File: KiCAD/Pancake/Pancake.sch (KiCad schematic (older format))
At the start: 40 parts, among them IC3 LF347N, J1 Conn_01x08_Male, J101 TB001-500-04BE, J102 TB001-500-03BE, J2 Conn_01x08_Male, J3 Conn_01x08_Male, J4 Conn_01x08_Male, J5 Conn_01x08_Male, J7 Conn_02x15_Top_Bottom

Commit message: Latest revision
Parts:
- IC3: symbol SamacSys_Parts:LF347N -> Pancake-rescue:LF347N-SamacSys_Parts
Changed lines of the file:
@@
 ADC0
 $Comp
-L SamacSys_Parts:LF347N IC3
+L Pancake-rescue:LF347N-SamacSys_Parts IC3
 U 1 1 612701DD
 P 3725 2975

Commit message: Lib updates and capacitor add. Simulation on power resistor working
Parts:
- added C101: 220nF, Capacitor_THT:CP_Radial_D16.0mm_P7.50mm, symbol Device:C
- IC3: footprint DIP794W56P254L1905H533Q14N -> SamacSys_Parts:DIP794W56P254L1905H533Q14N; symbol Pancake-rescue:LF347N-SamacSys_Parts -> SamacSys_Parts:LF347N
- J101: footprint TB00150004BE -> SamacSys_Parts:TB00150004BE; symbol Pancake-rescue:TB001-500-04BE-SamacSys_Parts -> SamacSys_Parts:TB001-500-04BE
- J102: footprint TB00150003BE -> SamacSys_Parts:TB00150003BE; symbol Pancake-rescue:TB001-500-03BE-SamacSys_Parts -> SamacSys_Parts:TB001-500-03BE
- R101: footprint TO508P438X1010X1539-2P -> SamacSys_Parts:TO508P438X1010X1539-2P; symbol Pancake-rescue:PWR220T-35-8R00F-SamacSys_Parts -> SamacSys_Parts:PWR220T-35-8R00F
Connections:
- wire segments 75 -> 79
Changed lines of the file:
@@
 Text Label 6500 7075 0    50   ~ 0
 AuxIn
-Text Label 4175 4625 2    50   ~ 0
+Text Label 4175 4475 2    50   ~ 0
 SPRKPos
 Text Label 8400 3625 2    50   ~ 0
 8VOut
-Text Label 4175 5575 2    50   ~ 0
+Text Label 4175 5775 2    50   ~ 0
 SPRKNeg
 Wire Wire Line
@@
 ADC0
 $Comp
-L Pancake-rescue:LF347N-SamacSys_Parts IC3
+L SamacSys_Parts:LF347N IC3
 U 1 1 612701DD
 P 3725 2975
 F 0 "IC3" H 4275 3240 50  0000 C CNN
 F 1 "LF347N" H 4275 3149 50  0000 C CNN
-F 2 "DIP794W56P254L1905H533Q14N" H 4675 3075 50  0001 L CNN
+F 2 "SamacSys_Parts:DIP794W56P254L1905H533Q14N" H 4675 3075 50  0001 L CNN
 F 3 "http://www.ti.com/lit/ds/symlink/lf347-n.pdf" H 4675 2975 50  0001 L CNN
 F 4 "Quad General-Purpose JFET-input Operational Amplifier" H 4675 2875 50  0001 L CNN "Description"
@@
 PresenceOut
 $Comp
-L Pancake-rescue:PWR220T-35-8R00F-SamacSys_Parts R101
+L SamacSys_Parts:PWR220T-35-8R00F R101
 U 1 1 614C8890
-P 4525 5425
-F 0 "R101" H 4875 5650 50  0000 C CNN
-F 1 "PWR220T-35-8R00F" H 4875 5559 50  0000 C CNN
-F 2 "TO508P438X1010X1539-2P" H 5075 5475 50  0001 L CNN
-F 3 "https://componentsearchengine.com/Datasheets/1/PWR220T-35-8R00F.pdf" H 5075 5375 50  0001 L CNN
-F 4 "Thick Film Resistors - Through Hole 8ohm 35W 1% TOL Thru Hole" H 5075 5275 50  0001 L CNN "Description"
-F 5 "4.38" H 5075 5175 50  0001 L CNN "Height"
-F 6 "Bourns" H 5075 5075 50  0001 L CNN "Manufacturer_Name"
-F 7 "PWR220T-35-8R00F" H 5075 4975 50  0001 L CNN "Manufacturer_Part_Number"
-F 8 "652-PWR220T-35-8R00F" H 5075 4875 50  0001 L CNN "Mouser Part Number"
-F 9 "http://www.mouser.com/Search/ProductDetail.aspx?qs=Zq5ylnUbLm6EF6%252bwjhnGig%3d%3d" H 5075 4775 50  0001 L CNN "Mouser Price/Stock"
-F 10 "" H 5075 4675 50  0001 L CNN "Arrow Part Number"
-F 11 "" H 5075 4575 50  0001 L CNN "Arrow Price/Stock"
-	1    4525 5425
+P 4525 5625
+F 0 "R101" H 4875 5850 50  0000 C CNN
+F 1 "PWR220T-35-8R00F" H 4875 5759 50  0000 C CNN
+F 2 "SamacSys_Parts:TO508P438X1010X1539-2P" H 5075 5675 50  0001 L CNN
+F 3 "https://componentsearchengine.com/Datasheets/1/PWR220T-35-8R00F.pdf" H 5075 5575 50  0001 L CNN
+F 4 "Thick Film Resistors - Through Hole 8ohm 35W 1% TOL Thru Hole" H 5075 5475 50  0001 L CNN "Description"
+F 5 "4.38" H 5075 5375 50  0001 L CNN "Height"
+F 6 "Bourns" H 5075 5275 50  0001 L CNN "Manufacturer_Name"
+F 7 "PWR220T-35-8R00F" H 5075 5175 50  0001 L CNN "Manufacturer_Part_Number"
+F 8 "652-PWR220T-35-8R00F" H 5075 5075 50  0001 L CNN "Mouser Part Number"
+F 9 "http://www.mouser.com/Search/ProductDetail.aspx?qs=Zq5ylnUbLm6EF6%252bwjhnGig%3d%3d" H 5075 4975 50  0001 L CNN "Mouser Price/Stock"
+F 10 "" H 5075 4875 50  0001 L CNN "Arrow Part Number"
+F 11 "" H 5075 4775 50  0001 L CNN "Arrow Price/Stock"
+	1    4525 5625
 	0    -1   -1   0
 $EndComp
@@
 $EndComp
 $Comp
-L Pancake-rescue:TB001-500-04BE-SamacSys_Parts J101
+L SamacSys_Parts:TB001-500-04BE J101
 U 1 1 6131A74D
 P 1300 4550
 F 0 "J101" H 1592 3985 50  0000 C CNN
 F 1 "TB001-500-04BE" H 1592 4076 50  0000 C CNN
-F 2 "TB00150004BE" H 1950 4650 50  0001 L CNN
+F 2 "SamacSys_Parts:TB00150004BE" H 1950 4650 50  0001 L CNN
 F 3 "https://componentsearchengine.com/Datasheets/1/TB001-500-04BE.pdf" H 1950 4550 50  0001 L CNN
 F 4 "Fixed Terminal Blocks Terminal block, screw type, 5.00, horizontal, 4 poles, CUI Blue, slotted screw, PCB mount" H 1950 4450 50  0001 L CNN "Description"
@@
 $EndComp
 Wire Wire Line
-	4900 4700 4525 4700
-Wire Wire Line
-	4525 4700 4525 4725
-Wire Wire Line
-	4525 5425 4900 5425
-Wire Wire Line
-	4175 4625 4525 4625
-Wire Wire Line
-	4525 4625 4525 4700
-Connection ~ 4525 4700
-Wire Wire Line
-	4175 5575 4525 5575
-Wire Wire Line
-	4525 5575 4525 5425
-Connection ~ 4525 5425
-$Comp
-L Pancake-rescue:TB001-500-03BE-SamacSys_Parts J102
+	4175 4475 4525 4475
+Wire Wire Line
+	4525 4475 4525 4550
+Wire Wire Line
+	4175 5775 4525 5775
+Wire Wire Line
+	4525 5775 4525 5625
+$Comp
+L SamacSys_Parts:TB001-500-03BE J102
 U 1 1 6151F148
 P 2600 4525
 F 0 "J102" H 2892 4060 50  0000 C CNN
 F 1 "TB001-500-03BE" H 2892 4151 50  0000 C CNN
-F 2 "TB00150003BE" H 3250 4625 50  0001 L CNN
+F 2 "SamacSys_Parts:TB00150003BE" H 3250 4625 50  0001 L CNN
 F 3 "https://www.cuidevices.com/product/resource/tb001-500.pdf" H 3250 4525 50  0001 L CNN
 F 4 "Fixed Terminal Blocks screw type, 5.00, horizontal, 3 poles, CUI Blue, slotted screw, PCB mount" H 3250 4425 50  0001 L CNN "Description"
@@
 	0    1    1    0
 $EndComp
+$Comp
+L Device:C C?
+U 1 1 613EF2BB
+P 4525 4700
+AR Path="/61024B6A/613EF2BB" Ref="C?"  Part="1"
+AR Path="/612AE90B/613EF2BB" Ref="C?"  Part="1"
+AR Path="/613EF2BB" Ref="C101"  Part="1"
+F 0 "C101" V 4273 4700 50  0000 C CNN
+F 1 "220nF" V 4364 4700 50  0000 C CNN
+F 2 "Capacitor_THT:CP_Radial_D16.0mm_P7.50mm" H 4563 4550 50  0001 C CNN
+F 3 "~" H 4525 4700 50  0001 C CNN
+	1    4525 4700
+	1    0    0    -1
+$EndComp
+Wire Wire Line
+	4525 4850 4525 4925
+Wire Wire Line
+	4900 4700 4825 4700
+Wire Wire Line
+	4825 4700 4825 4475
+Wire Wire Line
+	4825 4475 4525 4475
+Connection ~ 4525 4475
+Wire Wire Line
+	4900 5425 4825 5425
+Wire Wire Line
+	4825 5425 4825 5775
+Wire Wire Line
+	4825 5775 4525 5775
+Connection ~ 4525 5775
 $EndSCHEMATC

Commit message: The traces is all that is left. we may fall into problems with mark with clearances, we will see.
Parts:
- removed R101: PWR220T-35-8R00F, SamacSys_Parts:TO508P438X1010X1539-2P, symbol SamacSys_Parts:PWR220T-35-8R00F
- added R85, R86: 10, Resistor_THT:R_Axial_Power_L48.0mm_W12.5mm_P55.88mm, symbol Device:R
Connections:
- wire segments 79 -> 85
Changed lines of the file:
@@
 ADC0
-$Comp
-L SamacSys_Parts:LF347N IC3
-U 1 1 612701DD
-P 3725 2975
-F 0 "IC3" H 4275 3240 50  0000 C CNN
-F 1 "LF347N" H 4275 3149 50  0000 C CNN
-F 2 "SamacSys_Parts:DIP794W56P254L1905H533Q14N" H 4675 3075 50  0001 L CNN
-F 3 "http://www.ti.com/lit/ds/symlink/lf347-n.pdf" H 4675 2975 50  0001 L CNN
-F 4 "Quad General-Purpose JFET-input Operational Amplifier" H 4675 2875 50  0001 L CNN "Description"
-F 5 "5.334" H 4675 2775 50  0001 L CNN "Height"
-F 6 "Texas Instruments" H 4675 2675 50  0001 L CNN "Manufacturer_Name"
-F 7 "LF347N" H 4675 2575 50  0001 L CNN "Manufacturer_Part_Number"
-F 8 "595-LF347N" H 4675 2475 50  0001 L CNN "Mouser Part Number"
-F 9 "https://www.mouser.co.uk/ProductDetail/Texas-Instruments/LF347N?qs=DcvZ7Fltd5zOlQRQ%252BiS7vA%3D%3D" H 4675 2375 50  0001 L CNN "Mouser Price/Stock"
-F 10 "LF347N" H 4675 2275 50  0001 L CNN "Arrow Part Number"
-F 11 "https://www.arrow.com/en/products/lf347n/texas-instruments" H 4675 2175 50  0001 L CNN "Arrow Price/Stock"
-	1    3725 2975
-	1    0    0    -1
-$EndComp
 $Comp
 L Device:R R?
@@
 Text Label 3775 1975 0    50   ~ 0
 PresenceOut
-$Comp
-L SamacSys_Parts:PWR220T-35-8R00F R101
-U 1 1 614C8890
-P 4525 5625
-F 0 "R101" H 4875 5850 50  0000 C CNN
-F 1 "PWR220T-35-8R00F" H 4875 5759 50  0000 C CNN
-F 2 "SamacSys_Parts:TO508P438X1010X1539-2P" H 5075 5675 50  0001 L CNN
-F 3 "https://componentsearchengine.com/Datasheets/1/PWR220T-35-8R00F.pdf" H 5075 5575 50  0001 L CNN
-F 4 "Thick Film Resistors - Through Hole 8ohm 35W 1% TOL Thru Hole" H 5075 5475 50  0001 L CNN "Description"
-F 5 "4.38" H 5075 5375 50  0001 L CNN "Height"
-F 6 "Bourns" H 5075 5275 50  0001 L CNN "Manufacturer_Name"
-F 7 "PWR220T-35-8R00F" H 5075 5175 50  0001 L CNN "Manufacturer_Part_Number"
-F 8 "652-PWR220T-35-8R00F" H 5075 5075 50  0001 L CNN "Mouser Part Number"
-F 9 "http://www.mouser.com/Search/ProductDetail.aspx?qs=Zq5ylnUbLm6EF6%252bwjhnGig%3d%3d" H 5075 4975 50  0001 L CNN "Mouser Price/Stock"
-F 10 "" H 5075 4875 50  0001 L CNN "Arrow Part Number"
-F 11 "" H 5075 4775 50  0001 L CNN "Arrow Price/Stock"
-	1    4525 5625
-	0    -1   -1   0
-$EndComp
 $Comp
 L power:+12V #PWR0116
@@
 Wire Wire Line
 	4175 5775 4525 5775
-Wire Wire Line
-	4525 5775 4525 5625
 $Comp
 L SamacSys_Parts:TB001-500-03BE J102
@@
 $EndComp
 Wire Wire Line
-	4525 4850 4525 4925
-Wire Wire Line
 	4900 4700 4825 4700
 Wire Wire Line
@@
 	4825 5775 4525 5775
 Connection ~ 4525 5775
+$Comp
+L SamacSys_Parts:LF347N IC3
+U 1 1 612701DD
+P 3725 2975
+F 0 "IC3" H 4275 3240 50  0000 C CNN
+F 1 "LF347N" H 4275 3149 50  0000 C CNN
+F 2 "SamacSys_Parts:DIP794W56P254L1905H533Q14N" H 4675 3075 50  0001 L CNN
+F 3 "http://www.ti.com/lit/ds/symlink/lf347-n.pdf" H 4675 2975 50  0001 L CNN
+F 4 "Quad General-Purpose JFET-input Operational Amplifier" H 4675 2875 50  0001 L CNN "Description"
+F 5 "5.334" H 4675 2775 50  0001 L CNN "Height"
+F 6 "Texas Instruments" H 4675 2675 50  0001 L CNN "Manufacturer_Name"
+F 7 "LF347N" H 4675 2575 50  0001 L CNN "Manufacturer_Part_Number"
+F 8 "595-LF347N" H 4675 2475 50  0001 L CNN "Mouser Part Number"
+F 9 "https://www.mouser.co.uk/ProductDetail/Texas-Instruments/LF347N?qs=DcvZ7Fltd5zOlQRQ%252BiS7vA%3D%3D" H 4675 2375 50  0001 L CNN "Mouser Price/Stock"
+F 10 "LF347N" H 4675 2275 50  0001 L CNN "Arrow Part Number"
+F 11 "https://www.arrow.com/en/products/lf347n/texas-instruments" H 4675 2175 50  0001 L CNN "Arrow Price/Stock"
+	1    3725 2975
+	1    0    0    -1
+$EndComp
+$Comp
+L Device:R R?
+U 1 1 61472647
+P 4525 5275
+AR Path="/61024B6A/61472647" Ref="R?"  Part="1"
+AR Path="/612AE90B/61472647" Ref="R?"  Part="1"
+AR Path="/61472647" Ref="R86"  Part="1"
+F 0 "R86" V 4318 5275 50  0000 C CNN
+F 1 "10" V 4409 5275 50  0000 C CNN
+F 2 "Resistor_THT:R_Axial_Power_L48.0mm_W12.5mm_P55.88mm" V 4455 5275 50  0001 C CNN
+F 3 "~" H 4525 5275 50  0001 C CNN
+	1    4525 5275
+	-1   0    0    1
+$EndComp
+$Comp
+L Device:R R?
+U 1 1 614731F4
+P 4225 5275
+AR Path="/61024B6A/614731F4" Ref="R?"  Part="1"
+AR Path="/612AE90B/614731F4" Ref="R?"  Part="1"
+AR Path="/614731F4" Ref="R85"  Part="1"
+F 0 "R85" V 4018 5275 50  0000 C CNN
+F 1 "10" V 4109 5275 50  0000 C CNN
+F 2 "Resistor_THT:R_Axial_Power_L48.0mm_W12.5mm_P55.88mm" V 4155 5275 50  0001 C CNN
+F 3 "~" H 4225 5275 50  0001 C CNN
+	1    4225 5275
+	-1   0    0    1
+$EndComp
+Wire Wire Line
+	4525 4850 4525 5050
+Wire Wire Line
+	4225 5125 4225 5050
+Wire Wire Line
+	4225 5050 4525 5050
+Connection ~ 4525 5050
+Wire Wire Line
+	4525 5050 4525 5125
+Wire Wire Line
+	4225 5425 4225 5525
+Wire Wire Line
+	4225 5525 4525 5525
+Wire Wire Line
+	4525 5425 4525 5525
+Connection ~ 4525 5525
+Wire Wire Line
+	4525 5525 4525 5775
 $EndSCHEMATC

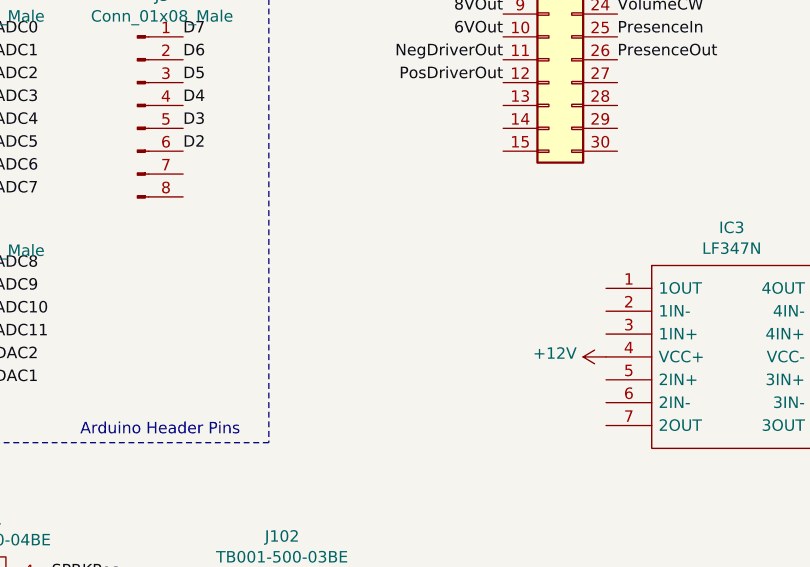
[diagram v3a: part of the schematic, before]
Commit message: LED for connection of power. I was not able to find the footprint for the 1206 SMD LED that is in the Senior design lab, but I was able to find one for a similar model. With that being said, the model is the same but the specs are different. I believe this shouldn't be a problem as I just needed the Surface mount plates that could hold the LED from the Lab. Will add the Active low LED tomorrow , need to look at what pins I can use for LED and 5V.
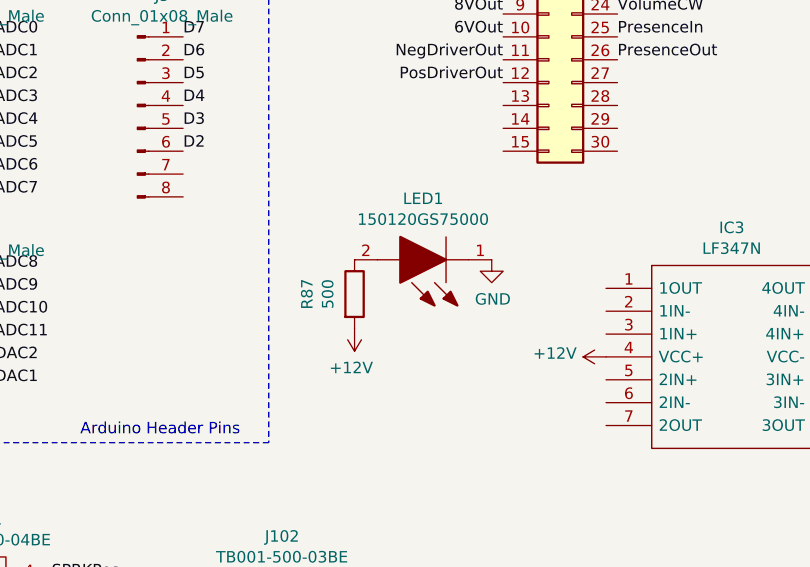
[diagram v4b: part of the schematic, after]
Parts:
- added LED1: 150120GS75000, LED_SMD:LED_1206_3216Metric, symbol SamacSys_Parts:150120GS75000
- added R87: 500, Resistor_THT:R_Axial_DIN0207_L6.3mm_D2.5mm_P10.16mm_Horizontal, symbol Device:R
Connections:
- net +12V: now also R87.2
- net GND: now also LED1.1
- new net: LED1.2, R87.1
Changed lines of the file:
@@
 Wire Wire Line
 	4525 5525 4525 5775
+$Comp
+L SamacSys_Parts:150120GS75000 LED1
+U 1 1 61471F94
+P 3225 2850
+F 0 "LED1" H 3525 2583 50  0000 C CNN
+F 1 "150120GS75000" H 3525 2674 50  0000 C CNN
+F 2 "LED_SMD:LED_1206_3216Metric" H 3725 3000 50  0001 L BNN
+F 3 "https://docs-emea.rs-online.com/webdocs/1302/0900766b81302e28.pdf" H 3725 2900 50  0001 L BNN
+F 4 "LED,Wurth Elektronik,150120GS75000 Wurth Elektronik 150120GS75000, WL-SMCW Series Green LED, 520 nm, 3016 (1206) Clear, Rectangle Lens SMD Package" H 3725 2800 50  0001 L BNN "Description"
+F 5 "0.78" H 3725 2700 50  0001 L BNN "Height"
+F 6 "Wurth Elektronik" H 3725 2600 50  0001 L BNN "Manufacturer_Name"
+F 7 "150120GS75000" H 3725 2500 50  0001 L BNN "Manufacturer_Part_Number"
+F 8 "710-150120GS75000" H 3725 2400 50  0001 L BNN "Mouser Part Number"
+F 9 "https://www.mouser.co.uk/ProductDetail/Wurth-Elektronik/150120GS75000?qs=LlUlMxKIyB3I3AMxrmBw4A%3D%3D" H 3725 2300 50  0001 L BNN "Mouser Price/Stock"
+F 10 "" H 3725 2200 50  0001 L BNN "Arrow Part Number"
+F 11 "" H 3725 2100 50  0001 L BNN "Arrow Price/Stock"
+	1    3225 2850
+	-1   0    0    1
+$EndComp
+$Comp
+L Device:R R?
+U 1 1 6147D62C
+P 2625 3000
+AR Path="/61024B6A/6147D62C" Ref="R?"  Part="1"
+AR Path="/612AE90B/6147D62C" Ref="R?"  Part="1"
+AR Path="/6147D62C" Ref="R87"  Part="1"
+F 0 "R87" V 2418 3000 50  0000 C CNN
+F 1 "500" V 2509 3000 50  0000 C CNN
+F 2 "Resistor_THT:R_Axial_DIN0207_L6.3mm_D2.5mm_P10.16mm_Horizontal" V 2555 3000 50  0001 C CNN
+F 3 "~" H 2625 3000 50  0001 C CNN
+	1    2625 3000
+	1    0    0    -1
+$EndComp
+$Comp
+L power:+12V #PWR01
+U 1 1 61484A8A
+P 2625 3150
+F 0 "#PWR01" H 2625 3000 50  0001 C CNN
+F 1 "+12V" H 2640 3323 50  0000 C CNN
+F 2 "" H 2625 3150 50  0001 C CNN
+F 3 "" H 2625 3150 50  0001 C CNN
+	1    2625 3150
+	-1   0    0    1
+$EndComp
+$Comp
+L power:GND #PWR02
+U 1 1 61485A09
+P 3225 2850
+F 0 "#PWR02" H 3225 2600 50  0001 C CNN
+F 1 "GND" H 3230 2677 50  0000 C CNN
+F 2 "" H 3225 2850 50  0001 C CNN
+F 3 "" H 3225 2850 50  0001 C CNN
+	1    3225 2850
+	1    0    0    -1
+$EndComp
 $EndSCHEMATC
